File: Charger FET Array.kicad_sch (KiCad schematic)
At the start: 32 parts, among them J9 To Battery Pack, Q21 CSD19531Q5A, Q22 CSD19531Q5A, Q23 CSD19531Q5A, Q24 CSD19531Q5A

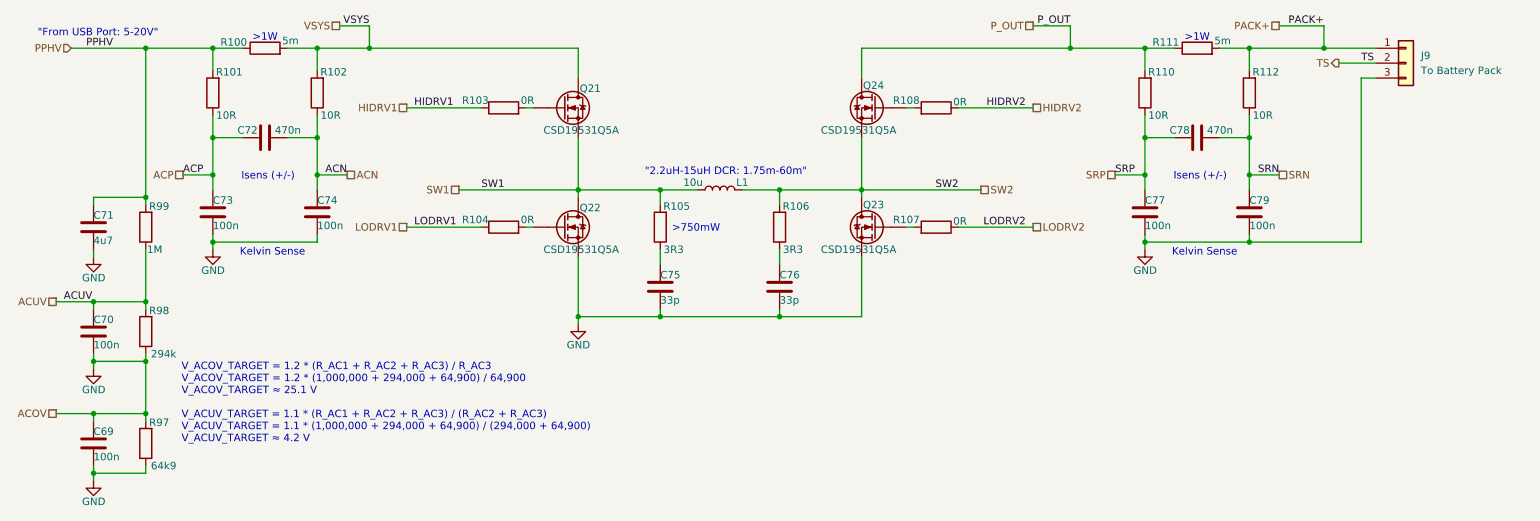
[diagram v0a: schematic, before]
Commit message: Fixed 5V Line
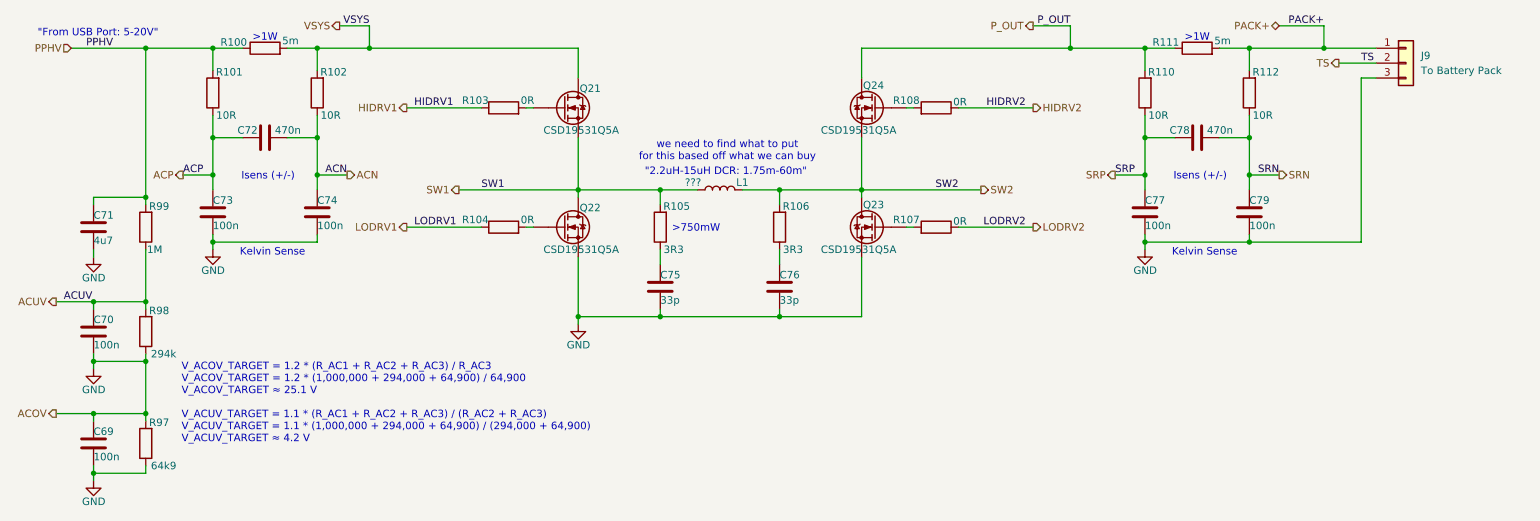
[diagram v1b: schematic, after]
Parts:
- L1: value 10u -> ???
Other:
- note added: "we need to find what to put for this based off what we can buy"
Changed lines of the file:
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@@
+		)
+	)
+	(text "we need to find what to put \nfor this based off what we can buy"
+		(exclude_from_sim no)
+		(at 140.97 101.346 0)
+		(effects
+			(font
+				(size 1.27 1.27)
+			)
 		)
 	)
@@
 	)
 	(hierarchical_label "VSYS"
-		(shape passive)
+		(shape output)
 		(at 74.93 80.01 180)
 		(effects
@@
 	)
 	(hierarchical_label "HIDRV2"
-		(shape passive)
+		(shape output)
 		(at 193.04 93.98 0)
 		(effects
@@
 	)
 	(hierarchical_label "LODRV2"
-		(shape passive)
+		(shape output)
 		(at 193.04 114.3 0)
 		(effects
@@
 	)
 	(hierarchical_label "ACOV"
-		(shape passive)
+		(shape output)
 		(at 26.67 146.05 180)
 		(effects
@@
 	)
 	(hierarchical_label "ACP"
-		(shape passive)
+		(shape output)
 		(at 48.26 105.41 180)
 		(effects
@@
 	)
 	(hierarchical_label "P_OUT"
-		(shape passive)
+		(shape output)
 		(at 193.04 80.01 180)
 		(effects
@@
 	)
 	(hierarchical_label "ACUV"
-		(shape passive)
+		(shape output)
 		(at 26.67 127 180)
 		(effects
@@
 	)
 	(hierarchical_label "SW1"
-		(shape passive)
+		(shape output)
 		(at 95.25 107.95 180)
 		(effects
@@
 	)
 	(hierarchical_label "LODRV1"
-		(shape passive)
+		(shape output)
 		(at 86.36 114.3 180)
 		(effects
@@
 	)
 	(hierarchical_label "HIDRV1"
-		(shape passive)
+		(shape output)
 		(at 86.36 93.98 180)
 		(effects
@@
 	)
 	(hierarchical_label "SW2"
-		(shape passive)
+		(shape output)
 		(at 184.15 107.95 0)
 		(effects
@@
 	)
 	(hierarchical_label "SRN"
-		(shape passive)
+		(shape output)
 		(at 234.95 105.41 0)
 		(effects
@@
 	)
 	(hierarchical_label "SRP"
-		(shape passive)
+		(shape output)
 		(at 207.01 105.41 180)
 		(effects
@@
 	)
 	(hierarchical_label "PACK+"
-		(shape passive)
+		(shape bidirectional)
 		(at 234.95 80.01 180)
 		(effects
@@
 	)
 	(hierarchical_label "ACN"
-		(shape passive)
+		(shape output)
 		(at 76.2 105.41 0)
 		(effects
@@
 			)
 		)
-		(property "Value" "10u"
+		(property "Value" "???"
 			(at 135.128 106.68 90)
 			(effects
